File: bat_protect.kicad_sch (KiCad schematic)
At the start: 19 parts, among them Q6 Q_NMOS_DGS, Q7 Q_NMOS_DGS, Q8 Q_NMOS_DGS, U16 BQ29209DRBR

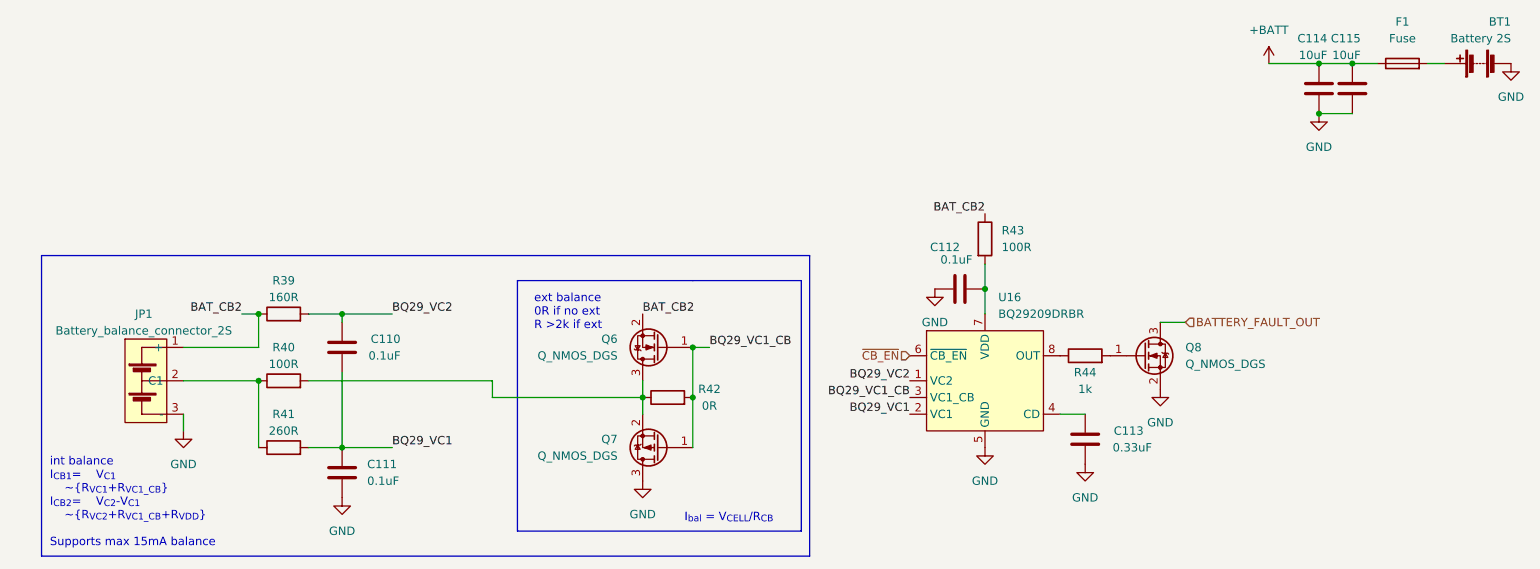
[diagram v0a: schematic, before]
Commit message: usb power source added, need to reassemble to 4-layers
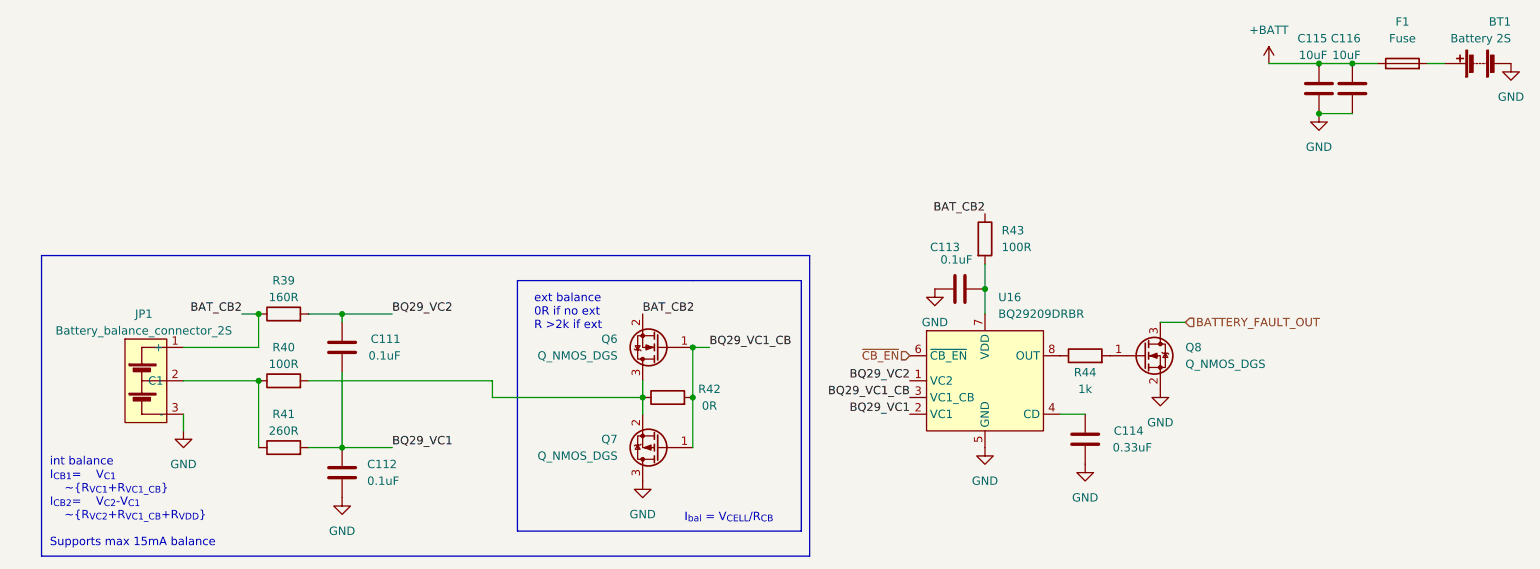
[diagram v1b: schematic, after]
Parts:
- renumbered C110 to C111, C111 to C112, C112 to C113, C113 to C114, C114 to C115, C115 to C116
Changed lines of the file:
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@@
   (symbol (lib_id "Device:C") (at 184.15 99.06 0) (mirror x) (unit 1)
     (in_bom yes) (on_board yes)
-    (property "Reference" "C113" (id 0) (at 193.04 97.79 0)
+    (property "Reference" "C114" (id 0) (at 193.04 97.79 0)
       (effects (font (size 1.27 1.27)) (justify right))
     )
@@
   (symbol (lib_id "Device:C") (at 71.12 104.14 0) (mirror y) (unit 1)
     (in_bom yes) (on_board yes)
-    (property "Reference" "C111" (id 0) (at 74.93 102.87 0)
+    (property "Reference" "C112" (id 0) (at 74.93 102.87 0)
       (effects (font (size 1.27 1.27)) (justify right))
     )
@@
   (symbol (lib_id "Device:C") (at 219.71 45.72 0) (mirror x) (unit 1)
     (in_bom yes) (on_board yes)
-    (property "Reference" "C114" (id 0) (at 220.98 38.1 0)
+    (property "Reference" "C115" (id 0) (at 220.98 38.1 0)
       (effects (font (size 1.27 1.27)) (justify right))
     )
@@
   (symbol (lib_id "Device:C") (at 224.79 45.72 0) (mirror x) (unit 1)
     (in_bom yes) (on_board yes)
-    (property "Reference" "C115" (id 0) (at 226.06 38.1 0)
+    (property "Reference" "C116" (id 0) (at 226.06 38.1 0)
       (effects (font (size 1.27 1.27)) (justify right))
     )
@@
   (symbol (lib_id "Device:C") (at 165.1 76.2 270) (mirror x) (unit 1)
     (in_bom yes) (on_board yes)
-    (property "Reference" "C112" (id 0) (at 165.1 69.85 90)
+    (property "Reference" "C113" (id 0) (at 165.1 69.85 90)
       (effects (font (size 1.27 1.27)) (justify right))
     )
@@
   (symbol (lib_id "Device:C") (at 71.12 85.09 0) (mirror x) (unit 1)
     (in_bom yes) (on_board yes)
-    (property "Reference" "C110" (id 0) (at 80.01 83.82 0)
+    (property "Reference" "C111" (id 0) (at 80.01 83.82 0)
       (effects (font (size 1.27 1.27)) (justify right))
     )

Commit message: done first iteration of pcb routing, slikscreen still broken
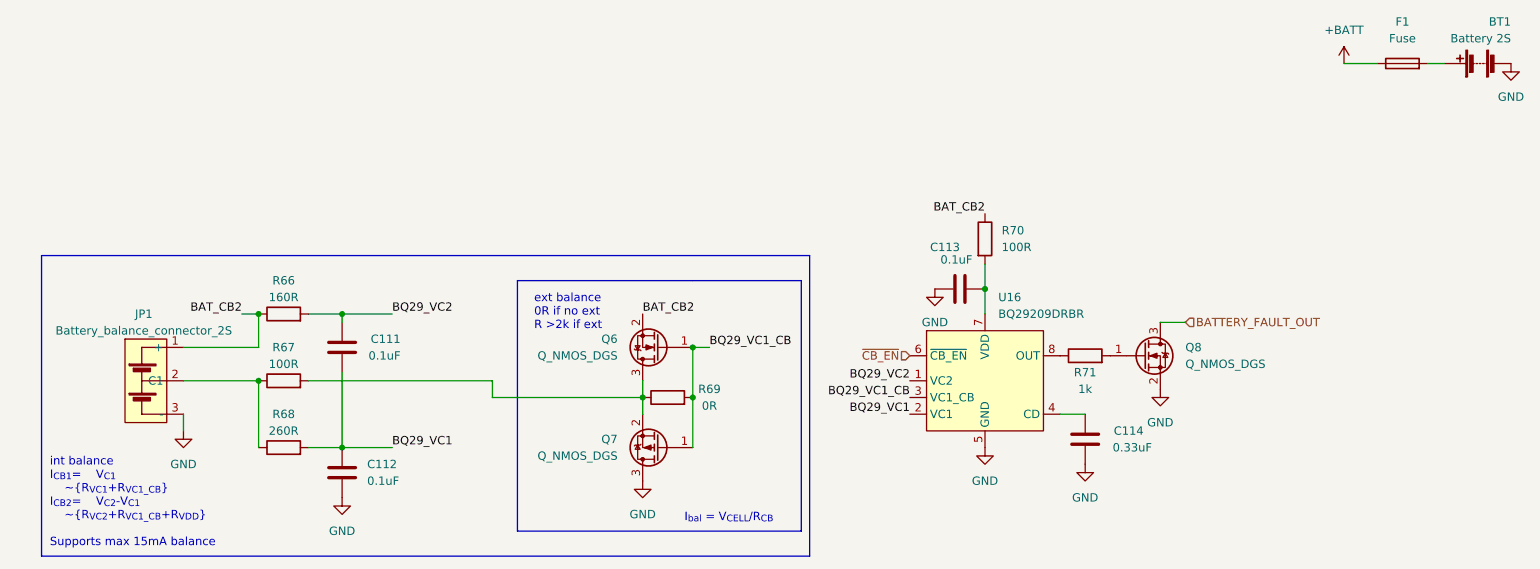
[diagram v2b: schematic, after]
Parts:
- removed C115, C116: 10uF, Capacitor_SMD:C_1206_3216Metric_Pad1.33x1.80mm_HandSolder, symbol Device:C
- renumbered R39 to R66, R40 to R67, R41 to R68, R42 to R69, R43 to R70, R44 to R71
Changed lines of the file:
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@@
 (kicad_sch (version 20211123) (generator eeschema)
   (paper "A4")
-  (junction (at 224.79 41.91) (diameter 0) (color 0 0 0 0)
-  )
   (junction (at 168.91 76.2) (diameter 0) (color 0 0 0 0)
   )
@@
   (junction (at 58.42 80.01) (diameter 0) (color 0 0 0 0)
   )
-  (junction (at 219.71 41.91) (diameter 0) (color 0 0 0 0)
-  )
   (junction (at 124.46 85.09) (diameter 0) (color 0 0 0 0)
   )
@@
   (junction (at 71.12 80.01) (diameter 0) (color 0 0 0 0)
   )
-  (junction (at 219.71 49.53) (diameter 0) (color 0 0 0 0)
-  )
   (wire (pts (xy 93.98 90.17) (xy 93.98 92.71))
     (stroke (width 0) (type default) (color 0 0 0 0))
@@
     (stroke (width 0) (type default) (color 0 0 0 0))
   )
-  (wire (pts (xy 212.09 41.91) (xy 219.71 41.91))
-    (stroke (width 0) (type default) (color 0 0 0 0))
-  )
   (wire (pts (xy 66.04 100.33) (xy 71.12 100.33))
     (stroke (width 0) (type default) (color 0 0 0 0))
@@
     (stroke (width 0) (type default) (color 0 0 0 0))
   )
-  (wire (pts (xy 219.71 41.91) (xy 224.79 41.91))
+  (wire (pts (xy 223.52 41.91) (xy 228.6 41.91))
     (stroke (width 0) (type default) (color 0 0 0 0))
   )
@@
     (stroke (width 0) (type default) (color 0 0 0 0))
   )
-  (wire (pts (xy 224.79 41.91) (xy 228.6 41.91))
-    (stroke (width 0) (type default) (color 0 0 0 0))
-  )
   (wire (pts (xy 168.91 72.39) (xy 168.91 76.2))
     (stroke (width 0) (type default) (color 0 0 0 0))
@@
   )
   (wire (pts (xy 78.74 100.33) (xy 71.12 100.33))
-    (stroke (width 0) (type default) (color 0 0 0 0))
-  )
-  (wire (pts (xy 219.71 49.53) (xy 224.79 49.53))
     (stroke (width 0) (type default) (color 0 0 0 0))
   )
@@
   (symbol (lib_id "power:GND") (at 46.99 97.79 0) (unit 1)
     (in_bom yes) (on_board yes) (fields_autoplaced)
-    (property "Reference" "#PWR0134" (id 0) (at 46.99 104.14 0)
+    (property "Reference" "#PWR0137" (id 0) (at 46.99 104.14 0)
       (effects (font (size 1.27 1.27)) hide)
     )
@@
   (symbol (lib_id "Device:R") (at 62.23 90.17 90) (unit 1)
     (in_bom yes) (on_board yes)
-    (property "Reference" "R40" (id 0) (at 62.23 85.09 90))
+    (property "Reference" "R67" (id 0) (at 62.23 85.09 90))
     (property "Value" "100R" (id 1) (at 62.23 87.63 90))
     (property "Footprint" "Resistor_THT:R_Box_L13.0mm_W4.0mm_P9.00mm" (id 2) (at 62.23 91.948 90)
@@
     (pin "2")
   )
-  (symbol (lib_id "power:+BATT") (at 212.09 41.91 0) (unit 1)
-    (in_bom yes) (on_board yes) (fields_autoplaced)
-    (property "Reference" "#PWR0141" (id 0) (at 212.09 45.72 0)
-      (effects (font (size 1.27 1.27)) hide)
-    )
-    (property "Value" "+BATT" (id 1) (at 212.09 36.83 0))
-    (property "Footprint" "" (id 2) (at 212.09 41.91 0)
-      (effects (font (size 1.27 1.27)) hide)
-    )
-    (property "Datasheet" "" (id 3) (at 212.09 41.91 0)
+  (symbol (lib_id "power:+BATT") (at 223.52 41.91 0) (unit 1)
+    (in_bom yes) (on_board yes) (fields_autoplaced)
+    (property "Reference" "#PWR0144" (id 0) (at 223.52 45.72 0)
+      (effects (font (size 1.27 1.27)) hide)
+    )
+    (property "Value" "+BATT" (id 1) (at 223.52 36.83 0))
+    (property "Footprint" "" (id 2) (at 223.52 41.91 0)
+      (effects (font (size 1.27 1.27)) hide)
+    )
+    (property "Datasheet" "" (id 3) (at 223.52 41.91 0)
       (effects (font (size 1.27 1.27)) hide)
     )
@@
   (symbol (lib_id "power:GND") (at 71.12 107.95 0) (unit 1)
     (in_bom yes) (on_board yes) (fields_autoplaced)
-    (property "Reference" "#PWR0135" (id 0) (at 71.12 114.3 0)
+    (property "Reference" "#PWR0138" (id 0) (at 71.12 114.3 0)
       (effects (font (size 1.27 1.27)) hide)
     )
@@
   (symbol (lib_id "power:GND") (at 168.91 100.33 0) (unit 1)
     (in_bom yes) (on_board yes) (fields_autoplaced)
-    (property "Reference" "#PWR0138" (id 0) (at 168.91 106.68 0)
+    (property "Reference" "#PWR0141" (id 0) (at 168.91 106.68 0)
       (effects (font (size 1.27 1.27)) hide)
     )
@@
     (pin "3")
   )
-  (symbol (lib_id "power:GND") (at 219.71 49.53 0) (unit 1)
-    (in_bom yes) (on_board yes) (fields_autoplaced)
-    (property "Reference" "#PWR0142" (id 0) (at 219.71 55.88 0)
-      (effects (font (size 1.27 1.27)) hide)
-    )
-    (property "Value" "GND" (id 1) (at 219.71 54.61 0))
-    (property "Footprint" "" (id 2) (at 219.71 49.53 0)
-      (effects (font (size 1.27 1.27)) hide)
-    )
-    (property "Datasheet" "" (id 3) (at 219.71 49.53 0)
-      (effects (font (size 1.27 1.27)) hide)
-    )
-    (pin "1")
-  )
   (symbol (lib_id "power:GND") (at 248.92 41.91 0) (unit 1)
     (in_bom yes) (on_board yes) (fields_autoplaced)
-    (property "Reference" "#PWR0143" (id 0) (at 248.92 48.26 0)
+    (property "Reference" "#PWR0146" (id 0) (at 248.92 48.26 0)
       (effects (font (size 1.27 1.27)) hide)
     )
@@
   (symbol (lib_id "Device:R") (at 62.23 80.01 90) (unit 1)
     (in_bom yes) (on_board yes)
-    (property "Reference" "R39" (id 0) (at 62.23 74.93 90))
+    (property "Reference" "R66" (id 0) (at 62.23 74.93 90))
     (property "Value" "160R" (id 1) (at 62.23 77.47 90))
     (property "Footprint" "Resistor_SMD:R_0603_1608Metric_Pad0.98x0.95mm_HandSolder" (id 2) (at 62.23 81.788 90)
@@
   (symbol (lib_id "power:GND") (at 161.29 76.2 0) (unit 1)
     (in_bom yes) (on_board yes) (fields_autoplaced)
-    (property "Reference" "#PWR0137" (id 0) (at 161.29 82.55 0)
+    (property "Reference" "#PWR0140" (id 0) (at 161.29 82.55 0)
       (effects (font (size 1.27 1.27)) hide)
     )
@@
   (symbol (lib_id "Device:R") (at 184.15 86.36 90) (unit 1)
     (in_bom yes) (on_board yes)
-    (property "Reference" "R44" (id 0) (at 184.15 88.9 90))
+    (property "Reference" "R71" (id 0) (at 184.15 88.9 90))
     (property "Value" "1k" (id 1) (at 184.15 91.44 90))
     (property "Footprint" "Resistor_SMD:R_0603_1608Metric_Pad0.98x0.95mm_HandSolder" (id 2) (at 184.15 88.138 90)
@@
   (symbol (lib_id "power:GND") (at 195.58 91.44 0) (unit 1)
     (in_bom yes) (on_board yes) (fields_autoplaced)
-    (property "Reference" "#PWR0140" (id 0) (at 195.58 97.79 0)
+    (property "Reference" "#PWR0143" (id 0) (at 195.58 97.79 0)
       (effects (font (size 1.27 1.27)) hide)
     )
@@
   (symbol (lib_id "power:GND") (at 184.15 102.87 0) (unit 1)
     (in_bom yes) (on_board yes) (fields_autoplaced)
-    (property "Reference" "#PWR0139" (id 0) (at 184.15 109.22 0)
+    (property "Reference" "#PWR0142" (id 0) (at 184.15 109.22 0)
       (effects (font (size 1.27 1.27)) hide)
     )
@@
     (pin "1")
   )
-  (symbol (lib_id "Device:C") (at 219.71 45.72 0) (mirror x) (unit 1)
-    (in_bom yes) (on_board yes)
-    (property "Reference" "C115" (id 0) (at 220.98 38.1 0)
-      (effects (font (size 1.27 1.27)) (justify right))
-    )
-    (property "Value" "10uF" (id 1) (at 220.98 40.64 0)
-      (effects (font (size 1.27 1.27)) (justify right))
-    )
-    (property "Footprint" "Capacitor_SMD:C_1206_3216Metric_Pad1.33x1.80mm_HandSolder" (id 2) (at 220.6752 41.91 0)
-      (effects (font (size 1.27 1.27)) hide)
-    )
-    (property "Datasheet" "~" (id 3) (at 219.71 45.72 0)
-      (effects (font (size 1.27 1.27)) hide)
-    )
-    (pin "1")
-    (pin "2")
-  )
-  (symbol (lib_id "Device:C") (at 224.79 45.72 0) (mirror x) (unit 1)
-    (in_bom yes) (on_board yes)
-    (property "Reference" "C116" (id 0) (at 226.06 38.1 0)
-      (effects (font (size 1.27 1.27)) (justify right))
-    )
-    (property "Value" "10uF" (id 1) (at 226.06 40.64 0)
-      (effects (font (size 1.27 1.27)) (justify right))
-    )
-    (property "Footprint" "Capacitor_SMD:C_1206_3216Metric_Pad1.33x1.80mm_HandSolder" (id 2) (at 225.7552 41.91 0)
-      (effects (font (size 1.27 1.27)) hide)
-    )
-    (property "Datasheet" "~" (id 3) (at 224.79 45.72 0)
-      (effects (font (size 1.27 1.27)) hide)
-    )
-    (pin "1")
-    (pin "2")
-  )
   (symbol (lib_id "Device:Q_NMOS_GSD") (at 119.38 85.09 180) (unit 1)
     (in_bom yes) (on_board yes) (fields_autoplaced)
@@
   (symbol (lib_id "Device:R") (at 62.23 100.33 90) (unit 1)
     (in_bom yes) (on_board yes)
-    (property "Reference" "R41" (id 0) (at 62.23 95.25 90))
+    (property "Reference" "R68" (id 0) (at 62.23 95.25 90))
     (property "Value" "260R" (id 1) (at 62.23 97.79 90))
     (property "Footprint" "Resistor_SMD:R_0603_1608Metric_Pad0.98x0.95mm_HandSolder" (id 2) (at 62.23 102.108 90)
@@
   (symbol (lib_id "power:GND") (at 116.84 105.41 0) (unit 1)
     (in_bom yes) (on_board yes) (fields_autoplaced)
-    (property "Reference" "#PWR0136" (id 0) (at 116.84 111.76 0)
+    (property "Reference" "#PWR0139" (id 0) (at 116.84 111.76 0)
       (effects (font (size 1.27 1.27)) hide)
     )
@@
   (symbol (lib_id "Device:R") (at 120.65 92.71 90) (unit 1)
     (in_bom yes) (on_board yes)
-    (property "Reference" "R42" (id 0) (at 127 91.44 90))
+    (property "Reference" "R69" (id 0) (at 127 91.44 90))
     (property "Value" "0R" (id 1) (at 127 93.98 90))
     (property "Footprint" "Resistor_SMD:R_0603_1608Metric_Pad0.98x0.95mm_HandSolder" (id 2) (at 120.65 94.488 90)
@@
   (symbol (lib_id "Device:R") (at 168.91 68.58 0) (unit 1)
     (in_bom yes) (on_board yes) (fields_autoplaced)
-    (property "Reference" "R43" (id 0) (at 171.45 67.3099 0)
-      (effects (font (size 1.27 1.27)) (justify left))
-    )
+    (property "Reference" "R70" (id 0) (at 171.45 67.3099 0)
+      (effects (font (size 1.27 1.27)) (justify left))
+    )

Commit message: mounting holes, fixes silkscreen
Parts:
- renumbered R66 to R65, R67 to R66, R68 to R67, R69 to R68, R70 to R69, R71 to R70
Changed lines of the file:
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@@
   (symbol (lib_id "Device:R") (at 62.23 90.17 90) (unit 1)
     (in_bom yes) (on_board yes)
-    (property "Reference" "R67" (id 0) (at 62.23 85.09 90))
+    (property "Reference" "R66" (id 0) (at 62.23 85.09 90))
     (property "Value" "100R" (id 1) (at 62.23 87.63 90))
     (property "Footprint" "Resistor_THT:R_Box_L13.0mm_W4.0mm_P9.00mm" (id 2) (at 62.23 91.948 90)
@@
   (symbol (lib_id "power:GND") (at 248.92 41.91 0) (unit 1)
     (in_bom yes) (on_board yes) (fields_autoplaced)
-    (property "Reference" "#PWR0146" (id 0) (at 248.92 48.26 0)
+    (property "Reference" "#PWR0145" (id 0) (at 248.92 48.26 0)
       (effects (font (size 1.27 1.27)) hide)
     )
@@
   (symbol (lib_id "Device:R") (at 62.23 80.01 90) (unit 1)
     (in_bom yes) (on_board yes)
-    (property "Reference" "R66" (id 0) (at 62.23 74.93 90))
+    (property "Reference" "R65" (id 0) (at 62.23 74.93 90))
     (property "Value" "160R" (id 1) (at 62.23 77.47 90))
     (property "Footprint" "Resistor_SMD:R_0603_1608Metric_Pad0.98x0.95mm_HandSolder" (id 2) (at 62.23 81.788 90)
@@
   (symbol (lib_id "Device:R") (at 184.15 86.36 90) (unit 1)
     (in_bom yes) (on_board yes)
-    (property "Reference" "R71" (id 0) (at 184.15 88.9 90))
+    (property "Reference" "R70" (id 0) (at 184.15 88.9 90))
     (property "Value" "1k" (id 1) (at 184.15 91.44 90))
     (property "Footprint" "Resistor_SMD:R_0603_1608Metric_Pad0.98x0.95mm_HandSolder" (id 2) (at 184.15 88.138 90)
@@
   (symbol (lib_id "Device:R") (at 62.23 100.33 90) (unit 1)
     (in_bom yes) (on_board yes)
-    (property "Reference" "R68" (id 0) (at 62.23 95.25 90))
+    (property "Reference" "R67" (id 0) (at 62.23 95.25 90))
     (property "Value" "260R" (id 1) (at 62.23 97.79 90))
     (property "Footprint" "Resistor_SMD:R_0603_1608Metric_Pad0.98x0.95mm_HandSolder" (id 2) (at 62.23 102.108 90)
@@
   (symbol (lib_id "Device:R") (at 120.65 92.71 90) (unit 1)
     (in_bom yes) (on_board yes)
-    (property "Reference" "R69" (id 0) (at 127 91.44 90))
+    (property "Reference" "R68" (id 0) (at 127 91.44 90))
     (property "Value" "0R" (id 1) (at 127 93.98 90))
     (property "Footprint" "Resistor_SMD:R_0603_1608Metric_Pad0.98x0.95mm_HandSolder" (id 2) (at 120.65 94.488 90)
@@
   (symbol (lib_id "Device:R") (at 168.91 68.58 0) (unit 1)
     (in_bom yes) (on_board yes) (fields_autoplaced)
-    (property "Reference" "R70" (id 0) (at 171.45 67.3099 0)
-      (effects (font (size 1.27 1.27)) (justify left))
-    )
+    (property "Reference" "R69" (id 0) (at 171.45 67.3099 0)
+      (effects (font (size 1.27 1.27)) (justify left))
+    )
